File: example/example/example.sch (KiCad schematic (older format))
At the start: 25 parts, among them K0 KEYSW, K1 KEYSW, K2 KEYSW, K3 KEYSW, K4 KEYSW, K5 KEYSW, K6 KEYSW, K7 KEYSW, U1 TEENSY2.0, U2 TLC5971PWP

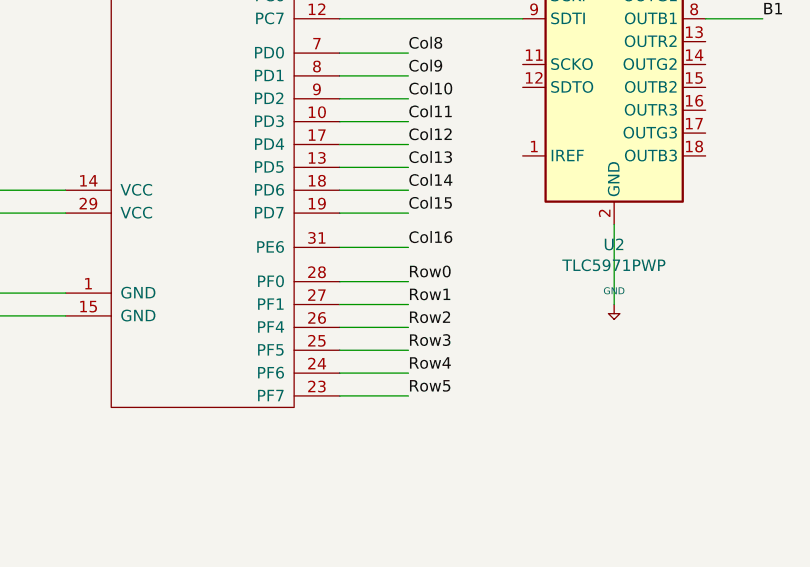
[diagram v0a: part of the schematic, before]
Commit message: update schematic
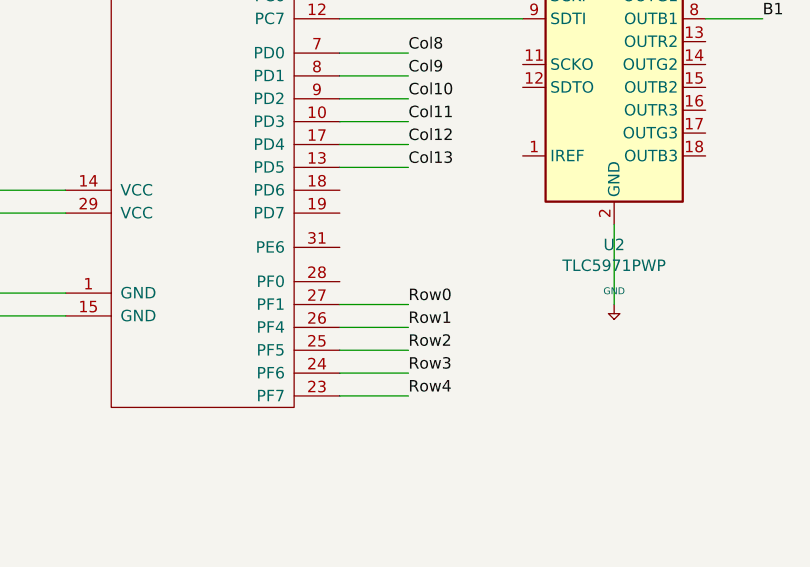
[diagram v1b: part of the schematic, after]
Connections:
- net Row5 is gone; now on net Row4: U1.23 (PF7)
- net Row0: now also U1.27 (PF1); no longer U1.28 (PF0)
- net Row1: now also U1.26 (PF4); no longer U1.27 (PF1)
- net Row2: now also U1.25 (PF5); no longer U1.26 (PF4)
- net Row3: now also U1.24 (PF6); no longer U1.25 (PF5)
- net Row4: no longer U1.24 (PF6)
- net Col14: no longer names the net of U1.18 (PD6)
- net Col15: no longer names the net of U1.19 (PD7)
- net Col16: no longer names the net of U1.31 (PE6)
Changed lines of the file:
@@
 	650  3450 650  3400
 Connection ~ 650  3400
-Text Label 2600 3300 0    50   ~ 0
+Text Label 2600 3400 0    50   ~ 0
 Row0
-Text Label 2600 3400 0    50   ~ 0
+Text Label 2600 3500 0    50   ~ 0
 Row1
-Text Label 2600 3500 0    50   ~ 0
+Text Label 2600 3600 0    50   ~ 0
 Row2
-Text Label 2600 3600 0    50   ~ 0
+Text Label 2600 3700 0    50   ~ 0
 Row3
-Text Label 2600 3700 0    50   ~ 0
+Text Label 2600 3800 0    50   ~ 0
 Row4
-Text Label 2600 3800 0    50   ~ 0
-Row5
-Text Label 2600 3000 0    50   ~ 0
-Col15
-Text Label 2600 2900 0    50   ~ 0
-Col14
 Text Label 2600 2800 0    50   ~ 0
 Col13
@@
 	2600 2800 2300 2800
 Wire Wire Line
-	2300 2900 2600 2900
-Wire Wire Line
-	2600 3000 2300 3000
-Wire Wire Line
-	2300 3300 2600 3300
-Wire Wire Line
 	2300 3400 2600 3400
 Wire Wire Line
-	2600 3500 2300 3500
+	2300 3500 2600 3500
 Wire Wire Line
-	2300 3600 2600 3600
+	2600 3600 2300 3600
 Wire Wire Line
 	2300 3700 2600 3700
@@
 	1    0    0    -1
 $EndComp
-Text Label 2600 3150 0    50   ~ 0
-Col16
-Wire Wire Line
-	2600 3150 2300 3150
 Wire Wire Line
 	2300 2150 3100 2150

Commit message: update schematic
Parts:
- D0, D1, D2, D3, D4, D5, D6, D7: symbol keyboard_parts:D -> example-rescue:D-keyboard_parts
- K0, K1, K2, K3, K4, K5, K6, K7: symbol keyboard_parts:KEYSW -> example-rescue:KEYSW-keyboard_parts
- U1: symbol keyboard_parts:TEENSY2.0 -> example-rescue:TEENSY2.0-keyboard_parts
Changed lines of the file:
@@
 Connection ~ 750  2950
 $Comp
-L keyboard_parts:GND #PWR?
+L example-rescue:GND-keyboard_parts #PWR?
 U 1 1 5DB147FE
 P 650 3400
@@
 	2300 3800 2600 3800
 $Comp
-L keyboard_parts:GND #PWR?
+L example-rescue:GND-keyboard_parts #PWR?
 U 1 1 5DB2C0BD
 P 3300 600
@@
 	3300 800  3300 600
 $Comp
-L keyboard_parts:TEENSY2.0 U1
+L example-rescue:TEENSY2.0-keyboard_parts U1
 U 1 1 5DB10FCA
 P 1700 2500
@@
 	3500 3050 3500 3400
 $Comp
-L keyboard_parts:GND #PWR?
+L example-rescue:GND-keyboard_parts #PWR?
 U 1 1 5DB23CD2
 P 3500 3400
@@
 	2300 2050 3100 2050
 $Comp
-L keyboard_parts:KEYSW K0
+L example-rescue:KEYSW-keyboard_parts K0
 U 1 1 5DB4E54F
 P 5700 1500
@@
 $EndComp
 $Comp
-L keyboard_parts:D D0
+L example-rescue:D-keyboard_parts D0
 U 1 1 5DB4FA1E
 P 5350 1700
@@
 Row0
 $Comp
-L keyboard_parts:KEYSW K1
+L example-rescue:KEYSW-keyboard_parts K1
 U 1 1 5DB58E5D
 P 5700 2000
@@
 $EndComp
 $Comp
-L keyboard_parts:D D1
+L example-rescue:D-keyboard_parts D1
 U 1 1 5DB58E63
 P 5350 2200
@@
 	5350 2000 5400 2000
 $Comp
-L keyboard_parts:KEYSW K2
+L example-rescue:KEYSW-keyboard_parts K2
 U 1 1 5DB5C4FE
 P 5700 2500
@@
 $EndComp
 $Comp
-L keyboard_parts:D D2
+L example-rescue:D-keyboard_parts D2
 U 1 1 5DB5C504
 P 5350 2700
@@
 	5350 2500 5400 2500
 $Comp
-L keyboard_parts:KEYSW K3
+L example-rescue:KEYSW-keyboard_parts K3
 U 1 1 5DB5EB78
 P 5700 3050
@@
 $EndComp
 $Comp
-L keyboard_parts:D D3
+L example-rescue:D-keyboard_parts D3
 U 1 1 5DB5EB7E
 P 5350 3250
@@
 Row3
 $Comp
-L keyboard_parts:KEYSW K4
+L example-rescue:KEYSW-keyboard_parts K4
 U 1 1 5DB823F7
 P 6550 1500
@@
 $EndComp
 $Comp
-L keyboard_parts:D D4
+L example-rescue:D-keyboard_parts D4
 U 1 1 5DB823FD
 P 6200 1700
@@
 Col1
 $Comp
-L keyboard_parts:KEYSW K5
+L example-rescue:KEYSW-keyboard_parts K5
 U 1 1 5DB8556D
 P 6550 2000
@@
 $EndComp
 $Comp
-L keyboard_parts:D D5
+L example-rescue:D-keyboard_parts D5
 U 1 1 5DB85573
 P 6200 2200
@@
 	6200 2000 6250 2000
 $Comp
-L keyboard_parts:KEYSW K6
+L example-rescue:KEYSW-keyboard_parts K6
 U 1 1 5DB865DD
 P 6550 2500
@@
 $EndComp
 $Comp
-L keyboard_parts:D D6
+L example-rescue:D-keyboard_parts D6
 U 1 1 5DB865E3
 P 6200 2700
@@
 	6200 2500 6250 2500
 $Comp
-L keyboard_parts:KEYSW K7
+L example-rescue:KEYSW-keyboard_parts K7
 U 1 1 5DB87746
 P 6550 3050
@@
 $EndComp
 $Comp
-L keyboard_parts:D D7
+L example-rescue:D-keyboard_parts D7
 U 1 1 5DB8774C
 P 6200 3250
@@
 	6650 5350 6650 6300
 $Comp
-L keyboard_parts:GND #PWR?
+L example-rescue:GND-keyboard_parts #PWR?
 U 1 1 5DC6258A
 P 5950 6600
@@
 $EndComp
 $Comp
-L keyboard_parts:GND #PWR?
+L example-rescue:GND-keyboard_parts #PWR?
 U 1 1 5DC62BAA
 P 5100 6600
